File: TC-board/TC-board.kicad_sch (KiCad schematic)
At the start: 13 parts, among them J1 DB15_Female, J2 PCIE-LP-01-01-F-DV-A-TR, J3 Conn_01x08_Male, J4 Conn_01x02_Male, J5 Conn_01x02_Male

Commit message: Progress on revising ground boards.
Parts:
- removed JP1, JP2, JP3: SolderJumper_3_Open, Jumper:SolderJumper-3_P2.0mm_Open_TrianglePad1.0x1.5mm, symbol Jumper:SolderJumper_3_Open
- removed JP4: SolderJumper_2_Open, Jumper:SolderJumper-2_P1.3mm_Open_TrianglePad1.0x1.5mm, symbol Jumper:SolderJumper_2_Open
- added J?: Conn_01x02_Male, symbol Connector:Conn_01x02_Male
- added J? (x3): Conn_01x03_Male, symbol Connector:Conn_01x03_Male
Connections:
- net CS1: now also J?.2 (Pin_2)
- net CS2: now also J?.2 (Pin_2)
- net CS3: now also J?.2 (Pin_2)
- net CS4: now also J?.1 (Pin_1)
- net TC1_CS: now also J?.1 (Pin_1)
- net TC2_CS: now also J?.1 (Pin_1)
- net TC3_CS: now also J?.1 (Pin_1)
- net TC4_CS: now also J?.2 (Pin_2), J?.3 (Pin_3), J?.3 (Pin_3), J?.3 (Pin_3)

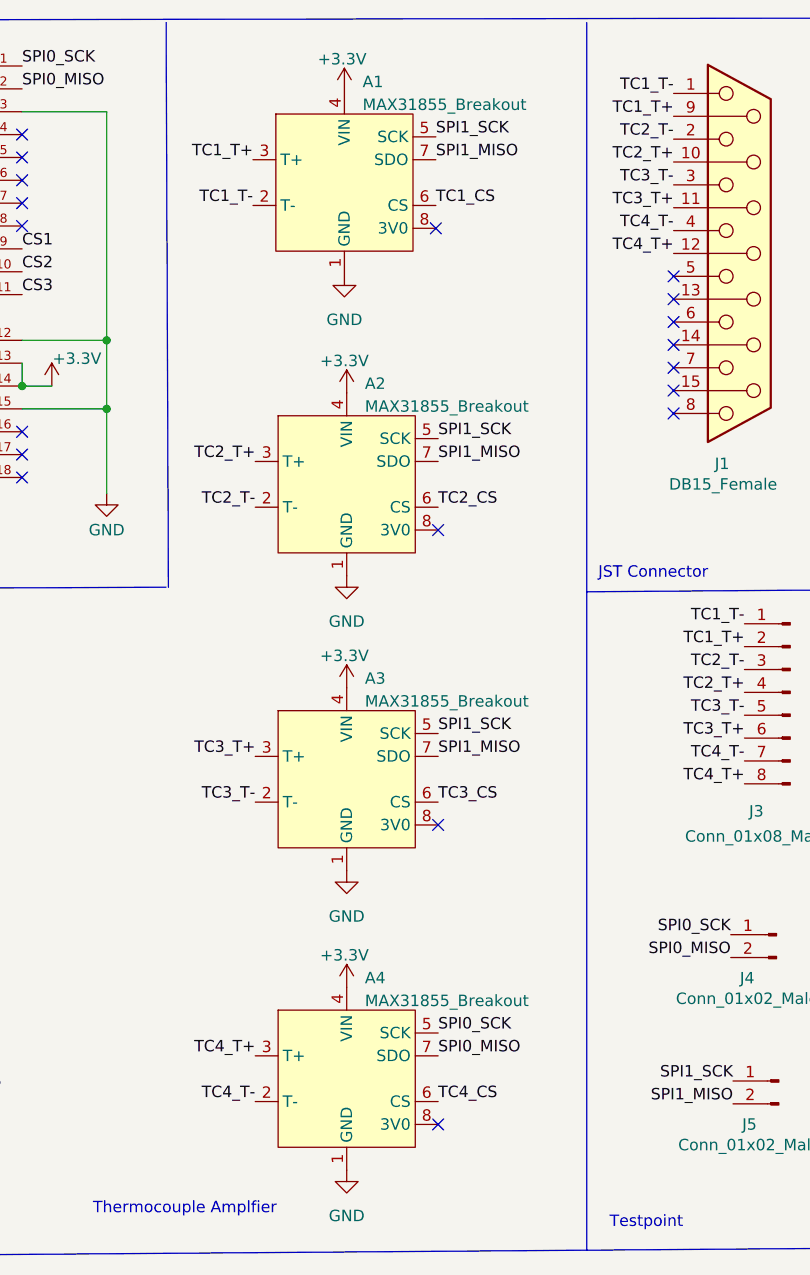
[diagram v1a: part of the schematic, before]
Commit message: Further revision. Two batteries system.
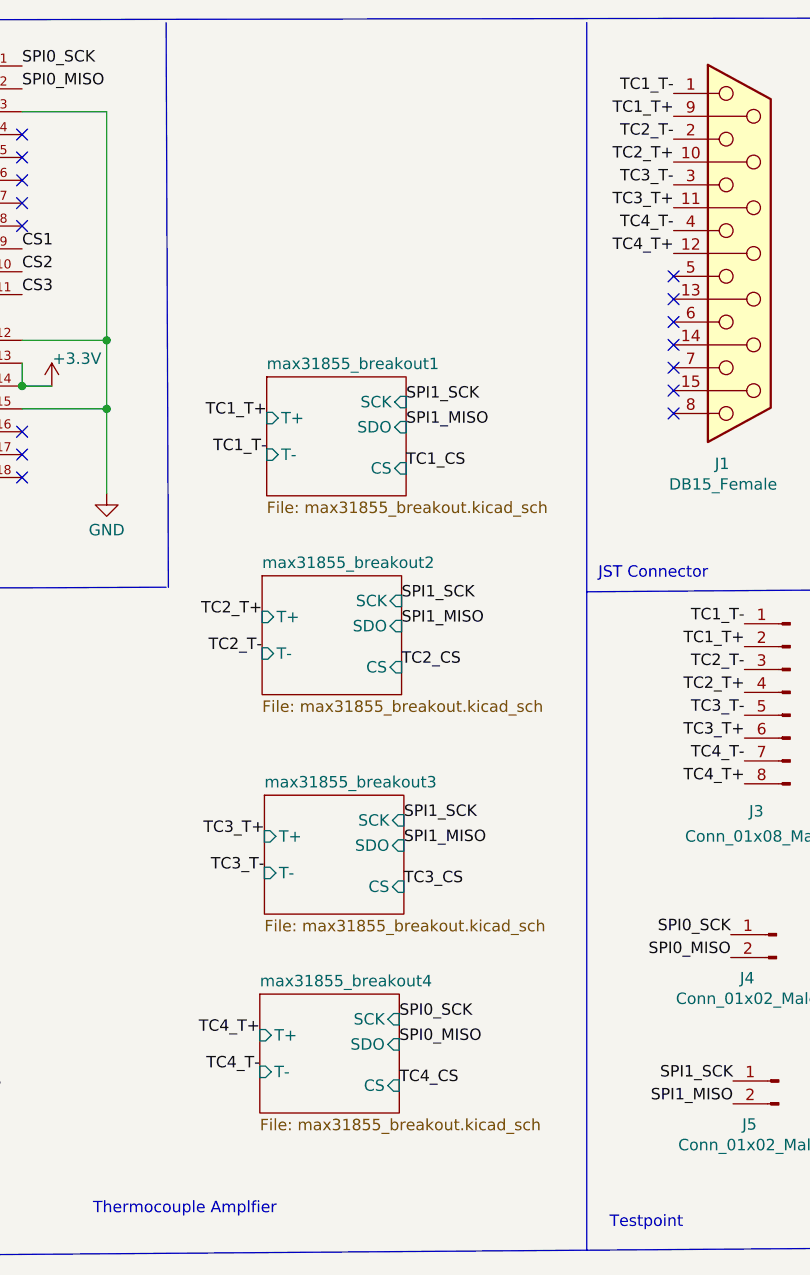
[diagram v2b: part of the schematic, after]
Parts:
- removed A1, A2, A3, A4: MAX31855_Breakout, MAX31855_Breakout:MAX31855_Breakout, symbol MAX31855_Breakout:MAX31855_Breakout
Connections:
- no-connect marks 30 -> 26
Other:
- added sheet max31855_breakout1 (max31855_breakout.kicad_sch)
- added sheet max31855_breakout2 (max31855_breakout.kicad_sch)
- added sheet max31855_breakout3 (max31855_breakout.kicad_sch)
- added sheet max31855_breakout4 (max31855_breakout.kicad_sch)

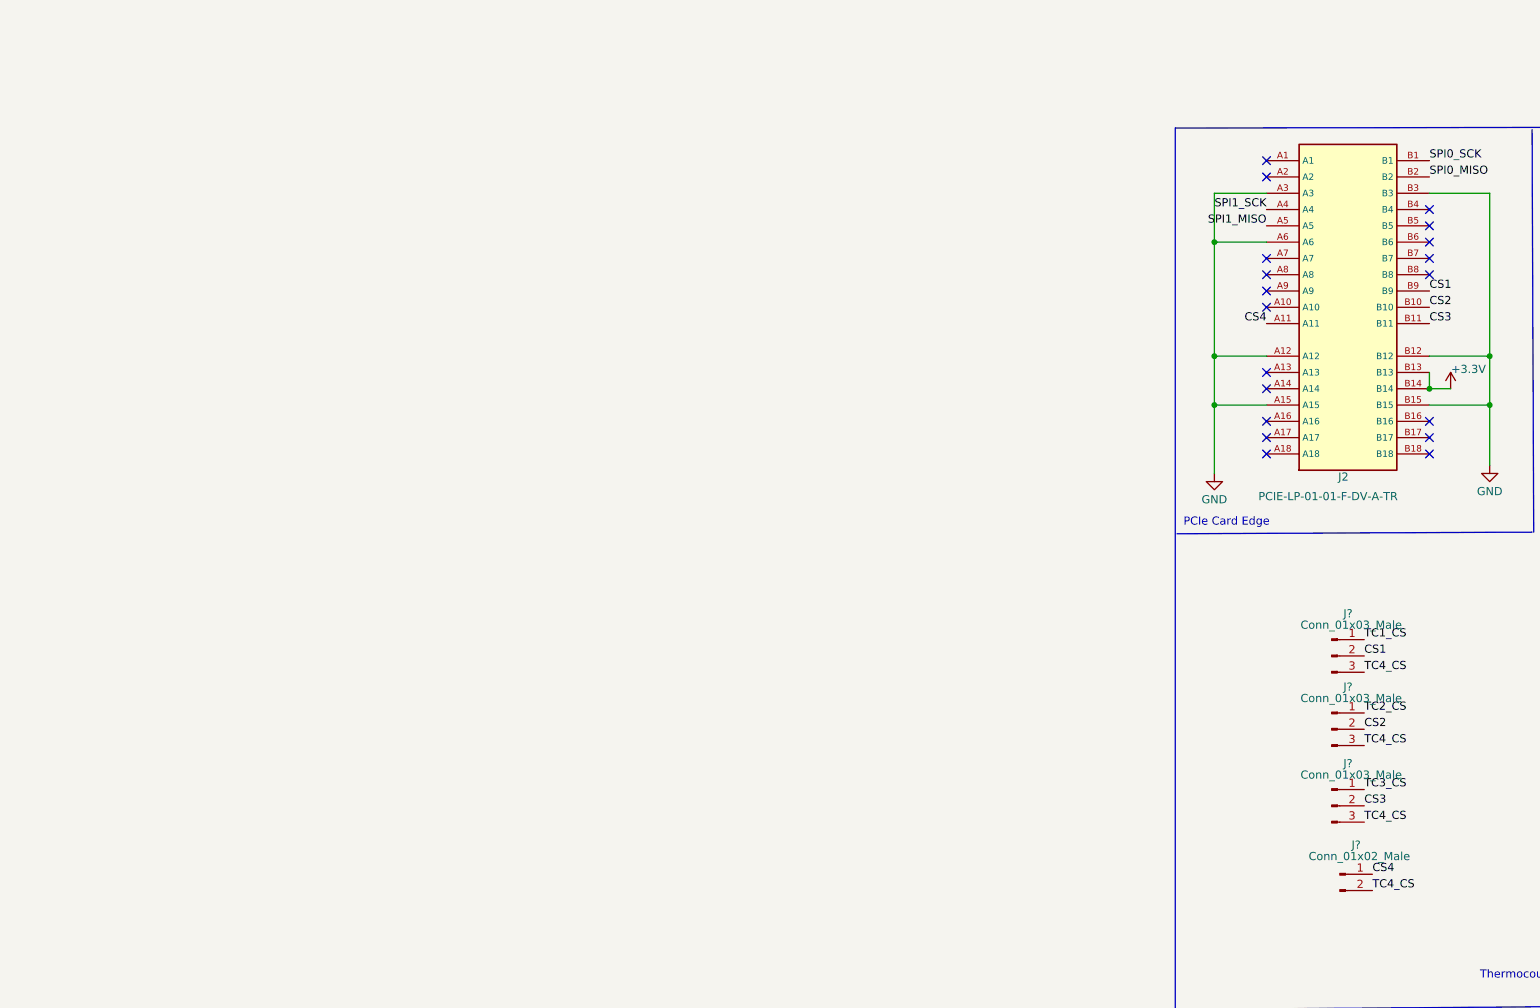
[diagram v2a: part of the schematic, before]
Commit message: Revising PCIe.
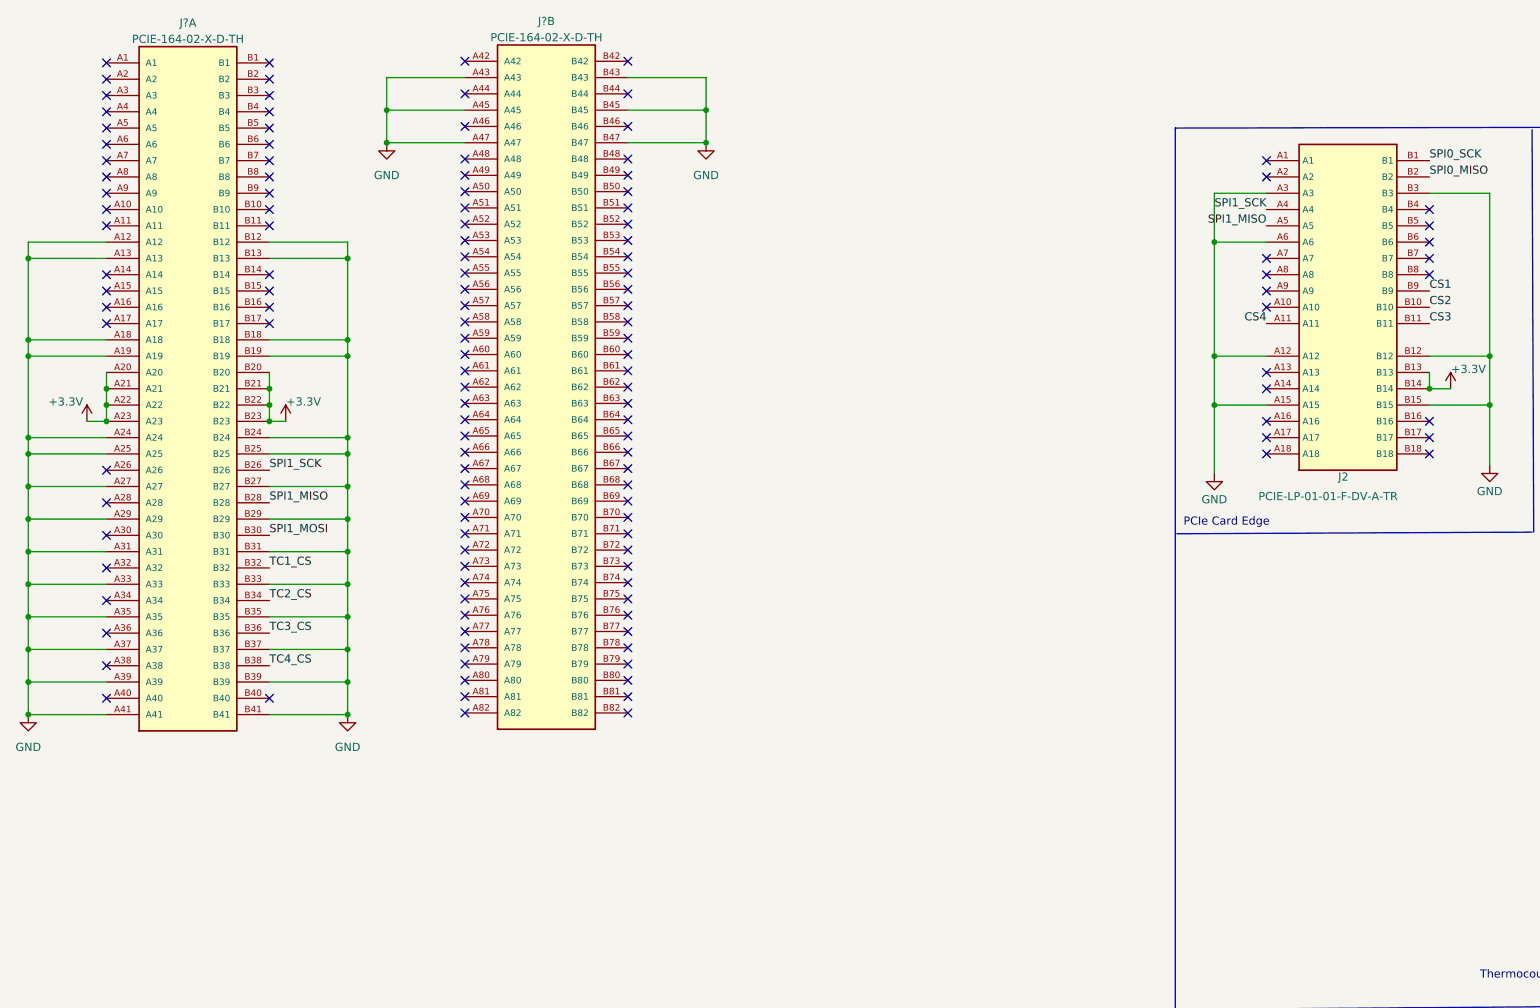
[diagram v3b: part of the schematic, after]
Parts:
- removed J?: Conn_01x02_Male, symbol Connector:Conn_01x02_Male
- removed J? (x3): Conn_01x03_Male, symbol Connector:Conn_01x03_Male
- added J? (x2): PCIE-164-02-X-D-TH, PCIE-164-02-X-D-TH:SAMTEC_PCIE-164-02-X-D-TH, symbol PCIE-164-02-X-D-TH:PCIE-164-02-X-D-TH
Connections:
- net +3.3V: now also J?.A20, J?.A21, J?.A22, J?.A23, J?.B20, J?.B21, J?.B22, J?.B23
- net GND: now also J?.A12, J?.A13, J?.A18, J?.A19, J?.A24, J?.A25, J?.A27, J?.A29, J?.A31, J?.A33, J?.A35, J?.A37, J?.A39, J?.A41, J?.A43, J?.A45, J?.A47, J?.B12, J?.B13, J?.B18, J?.B19, J?.B24, J?.B25, J?.B27, J?.B29, J?.B31, J?.B33, J?.B35, J?.B37, J?.B39, J?.B41, J?.B43, J?.B45, J?.B47
- net SPI1_MISO: now also J?.B28
- net SPI1_SCK: now also J?.B26
- net TC1_CS: now also J?.B32
- net TC2_CS: now also J?.B34
- net TC3_CS: now also J?.B36
- net TC4_CS: now also J?.B38
- new net SPI1_MOSI: J?.B30
- no-connect marks 26 -> 141

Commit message: Ironing out small details, changed pcf8575 to IC instead of breakout.
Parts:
- removed J2: PCIE-LP-01-01-F-DV-A-TR, Connector_PCBEdge:BUS_PCIexpress_x1, symbol PCIE_Card_Edge:PCIE-LP-01-01-F-DV-A-TR_(card_edge)
- removed J4: Conn_01x02_Male, Connector_PinHeader_1.27mm:PinHeader_1x02_P1.27mm_Vertical, symbol Connector:Conn_01x02_Male
- J3: footprint Connector_PinHeader_1.27mm:PinHeader_1x08_P1.27mm_Vertical -> Connector_PinHeader_2.54mm:PinHeader_1x02_P2.54mm_Vertical
- J5: footprint Connector_PinHeader_1.27mm:PinHeader_1x02_P1.27mm_Vertical -> Connector_PinHeader_2.54mm:PinHeader_1x02_P2.54mm_Vertical
- gave numbers to parts that had none: 1
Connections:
- net SPI1_MOSI: no longer names the net of J2.B30
- no-connect marks 141 -> 123
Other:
- moved on the sheet: J1, J2A, J2B, J3, J5
